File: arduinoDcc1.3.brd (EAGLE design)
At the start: 50 x 85 mm, 37 parts, among them IC1 7812TV, T2 2N2222, X1 MKDSN1,5/3-5,08, X2 MKDSN1,5/2-5,08, X3 MKDSN1,5/2-5,08, X4 MKDSN1,5/2-5,08, X5 MKDSN1,5/2-5,08, X6 MKDSN1,5/2-5,08, X7 MKDSN1,5/2-5,08, X8 MKDSN1,5/2-5,08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

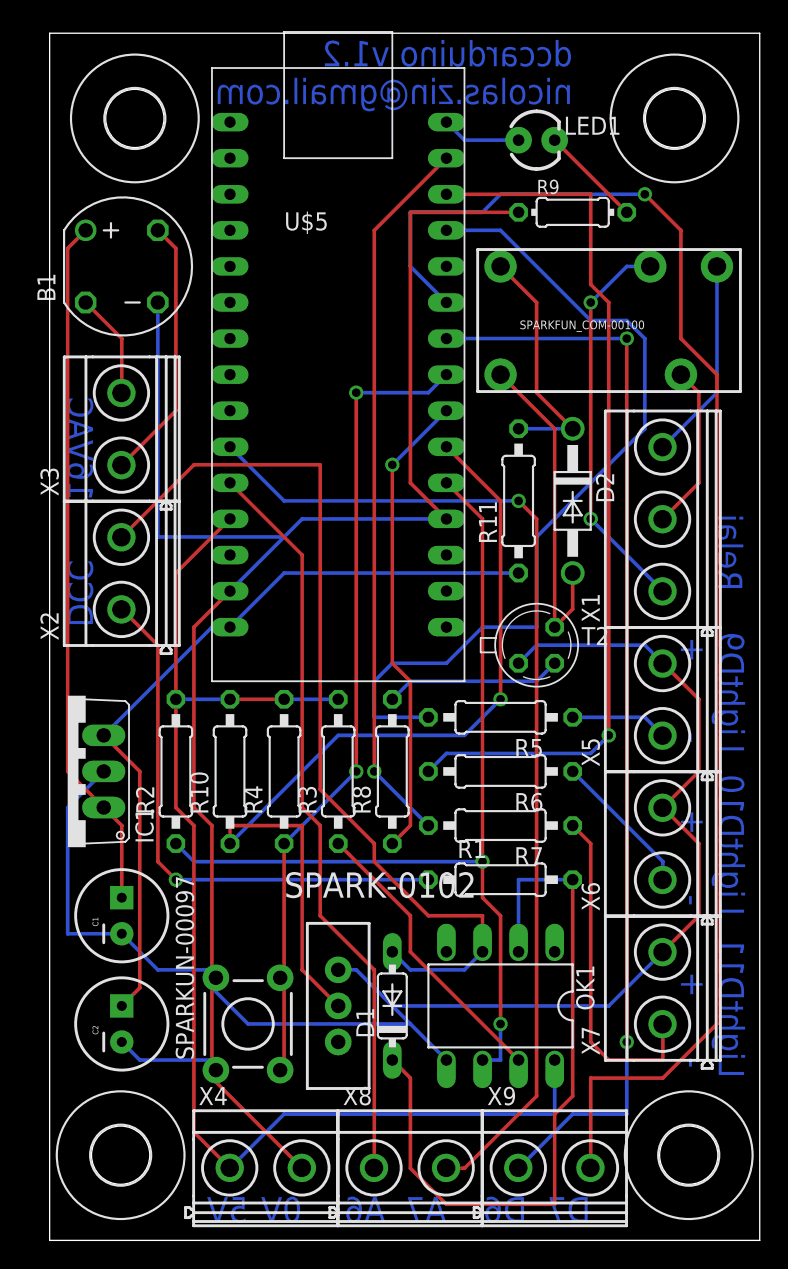
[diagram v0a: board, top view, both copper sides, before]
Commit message: change voltage regulator to swtiching power supply
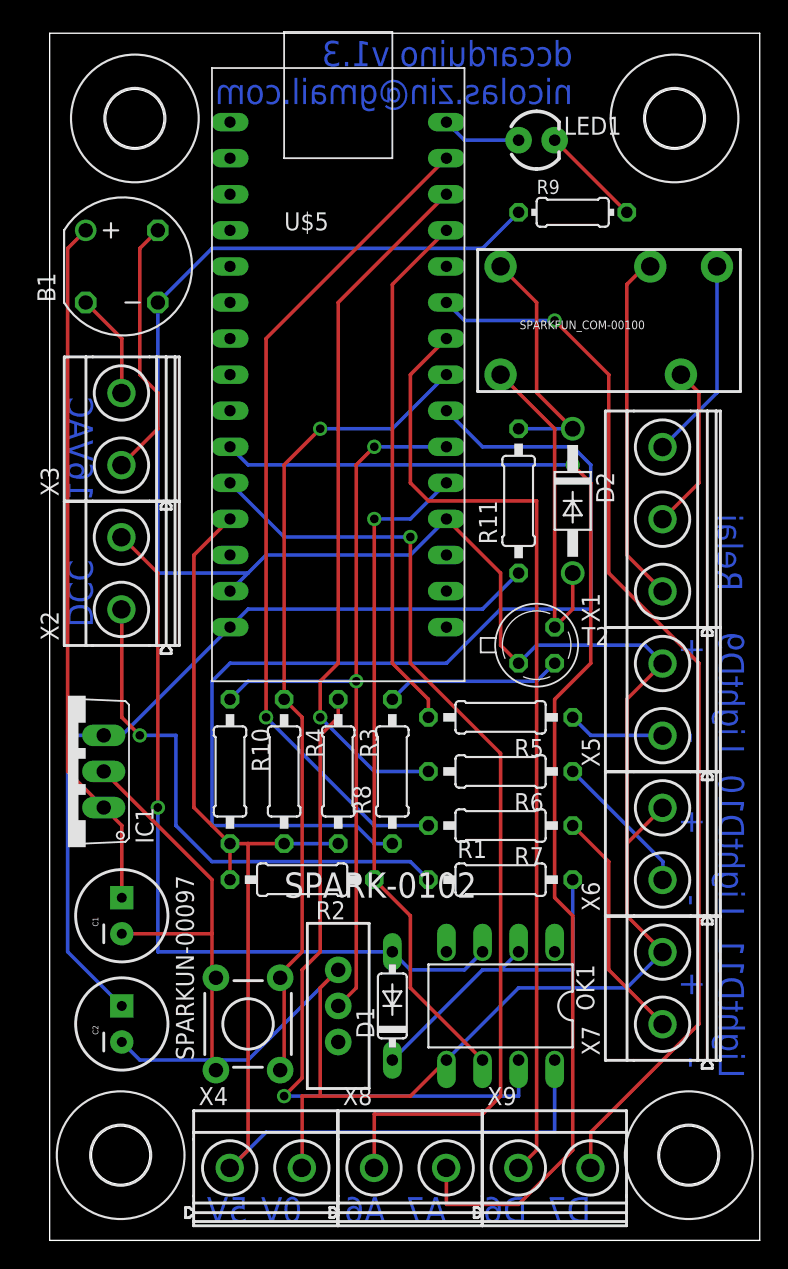
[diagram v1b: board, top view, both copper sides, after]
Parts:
- C1: value 220 uF -> 330 uF
- moved R2 11.7 mm to (17.8, 25.4), turned to 180 degrees
- turned R10 to 270 degrees
- turned R3 to 270 degrees
- turned R4 to 270 degrees
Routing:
- net N$12: track 33.1 -> 74.1 mm, vias 1 -> 0
- net N$2: track 51.6 -> 23.5 mm
- net N$7: track 20.5 -> 48.6 mm, vias 0 -> 1
- net N$20: track 101.8 -> 75.2 mm
- net N$16: track 60.0 -> 36.9 mm
- net N$6: track 65.6 -> 47.4 mm, vias 2 -> 1
- net GND: track 232.7 -> 214.4 mm
- net N$21: track 52.5 -> 69.5 mm, vias 0 -> 1
- net N$22: track 72.8 -> 88.1 mm
- net N$15: track 62.5 -> 49.7 mm
- net N$3: track 64.8 -> 54.2 mm, vias 0 -> 1
- net N$14: track 50.7 -> 59.2 mm
- net N$19: track 76.5 -> 68.2 mm, vias 2 -> 0
- net N$4: track 62.7 -> 54.9 mm, vias 1 -> 2
- net N$27: track 23.9 -> 16.6 mm
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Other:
- board text added: "dccarduino v1.3 nicolas.zin@gmail.com"
- board text removed: "dccarduino v1.2 nicolas.zin@gmail.com"

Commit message: new version 1.3, with DC-DC converter instead of voltage regulator
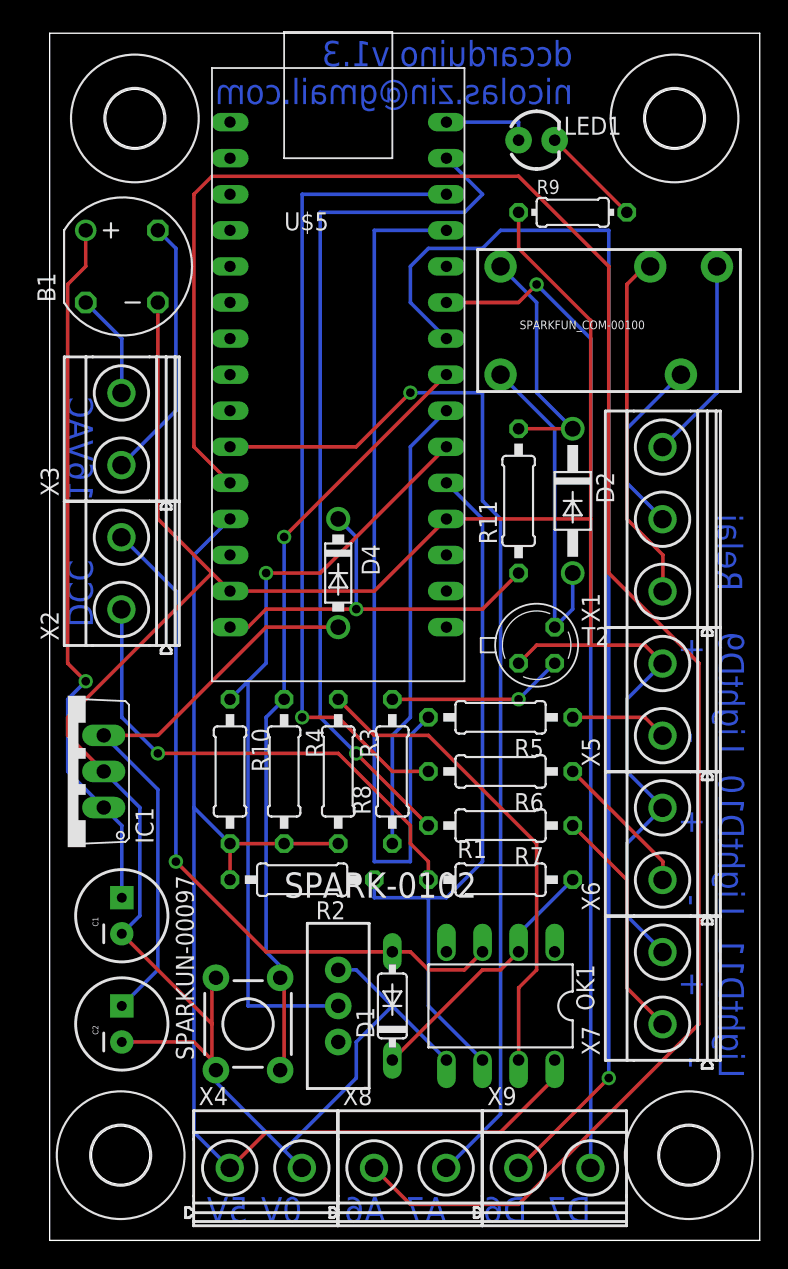
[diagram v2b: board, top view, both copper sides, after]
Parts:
- added D4: 1N5817-B, diode:DO41-7.6
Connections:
- new net N$31: D4.C, R11.1, U$5.P$15
- net N$28: now also D4.A; no longer R11.1, U$5.P$15
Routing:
- net N$21: track 69.5 -> 138.9 mm, vias 1 -> 0
- net N$12: track 74.1 -> 32.1 mm
- net N$31: track 0.00 -> 28.8 mm, vias 0 -> 1
- net N$16: track 36.9 -> 62.8 mm
- net N$19: track 68.2 -> 89.9 mm, vias 0 -> 1
- net N$28: track 57.1 -> 41.3 mm
- net N$7: track 48.6 -> 33.9 mm, vias 1 -> 0
- net N$22: track 88.1 -> 76.1 mm
- net GND: track 214.4 -> 206.3 mm
- net N$15: track 49.7 -> 57.5 mm
- net N$2: track 23.5 -> 18.7 mm
- net N$20: track 75.2 -> 70.7 mm
- net N$3: track 54.2 -> 49.7 mm
- net N$6: track 47.4 -> 50.7 mm, vias 1 -> 0
- net N$18: track 57.9 -> 54.9 mm
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
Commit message: update BOM
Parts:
- R5, R6, R7: value 400 -> 200
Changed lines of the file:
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@@
 <?xml version="1.0" encoding="utf-8"?>
 <!DOCTYPE eagle SYSTEM "eagle.dtd">
-<eagle version="6.6.0">
+<eagle version="7.6.0">
 <drawing>
 <settings>
@@
 <pass name="Default">
 <param name="RoutingGrid" value="50mil"/>
+<param name="AutoGrid" value="1"/>
+<param name="Efforts" value="0"/>
+<param name="TopRouterVariant" value="1"/>
 <param name="tpViaShape" value="round"/>
 <param name="PrefDir.1" value="*"/>
@@
 <attribute name="SPICEPREFIX" value="R" x="33.02" y="52.07" size="1.778" layer="27" rot="R90" display="off"/>
 </element>
-<element name="R5" library="eagle-ltspice" package="0207/10" value="400" x="31.75" y="36.83" rot="R180">
+<element name="R5" library="eagle-ltspice" package="0207/10" value="200" x="31.75" y="36.83" rot="R180">
 <attribute name="SPICEMODEL" value="NONE" x="31.75" y="36.83" size="1.778" layer="27" rot="R180" display="off"/>
 <attribute name="SPICEPREFIX" value="R" x="31.75" y="36.83" size="1.778" layer="27" rot="R180" display="off"/>
 </element>
-<element name="R6" library="eagle-ltspice" package="0207/10" value="400" x="31.75" y="33.02" rot="R180">
+<element name="R6" library="eagle-ltspice" package="0207/10" value="200" x="31.75" y="33.02" rot="R180">
 <attribute name="SPICEMODEL" value="NONE" x="31.75" y="33.02" size="1.778" layer="27" rot="R180" display="off"/>
 <attribute name="SPICEPREFIX" value="R" x="31.75" y="33.02" size="1.778" layer="27" rot="R180" display="off"/>
 </element>
-<element name="R7" library="eagle-ltspice" package="0207/10" value="400" x="31.75" y="29.21" rot="R180">
+<element name="R7" library="eagle-ltspice" package="0207/10" value="200" x="31.75" y="29.21" rot="R180">
 <attribute name="SPICEMODEL" value="NONE" x="31.75" y="29.21" size="1.778" layer="27" rot="R180" display="off"/>
 <attribute name="SPICEPREFIX" value="R" x="31.75" y="29.21" size="1.778" layer="27" rot="R180" display="off"/>
